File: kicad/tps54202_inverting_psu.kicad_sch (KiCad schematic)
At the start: 16 parts, among them J6 PowerConnector, J7 PowerConnector, J8 PowerConnector, U6 LM2611AMF/NOPB

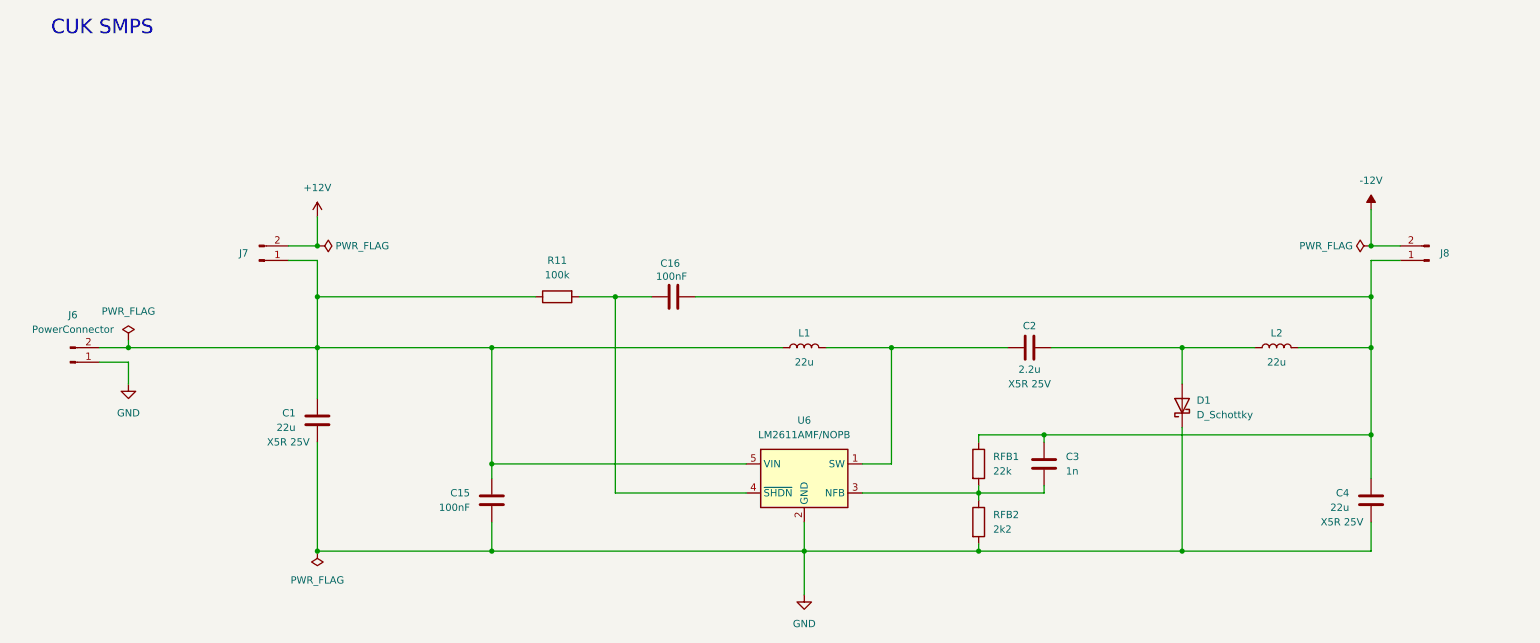
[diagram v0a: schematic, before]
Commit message: updated schematic to use TPS54202
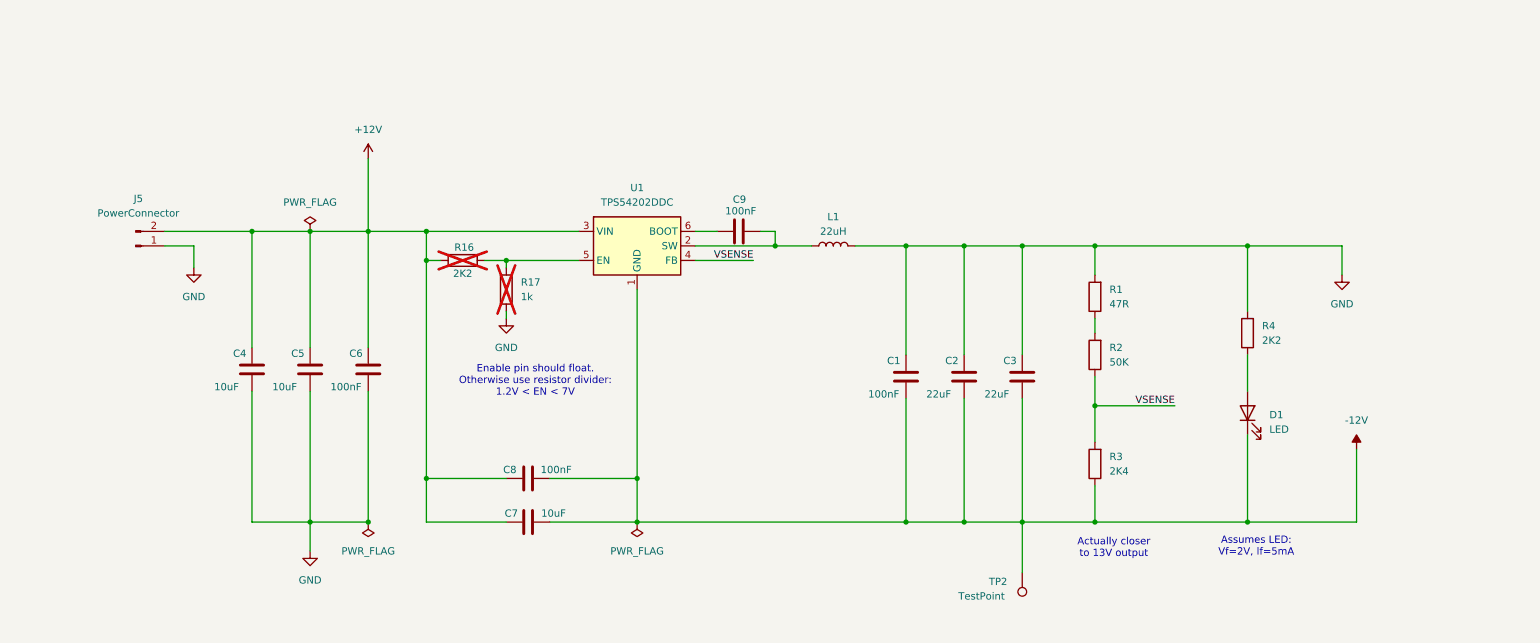
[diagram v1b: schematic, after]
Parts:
- removed C15, C16: 100nF, Capacitor_SMD:C_0603_1608Metric_Pad1.08x0.95mm_HandSolder, symbol Device:C
- removed D1: D_Schottky, Diode_SMD:D_PowerDI-123, symbol Device:D_Schottky
- removed J6: PowerConnector, Connector_Molex:Molex_KK-254_AE-6410-02A_1x02_P2.54mm_Vertical, symbol Connector:Conn_01x02_Pin
- removed J7, J8: PowerConnector, Connector_PinHeader_2.54mm:PinHeader_1x02_P2.54mm_Vertical, symbol Connector:Conn_01x02_Pin
- removed L2: 22u, Inductor_SMD:L_Ferrocore_DLG-0403, symbol Device:L
- removed R11: 100k, Resistor_SMD:R_0805_2012Metric_Pad1.20x1.40mm_HandSolder, symbol Device:R
- removed RFB1: 22k, Resistor_SMD:R_0805_2012Metric_Pad1.20x1.40mm_HandSolder, symbol Device:R
- removed RFB2: 2k2, Resistor_SMD:R_0805_2012Metric_Pad1.20x1.40mm_HandSolder, symbol Device:R
- removed U6: LM2611AMF/NOPB, Package_TO_SOT_SMD:SOT-23-5, symbol Regulator_Switching:LM2611xMF
- added C5, C7: 10uF, Capacitor_SMD:C_0805_2012Metric_Pad1.18x1.45mm_HandSolder, symbol Device:C
- added C6, C8, C9: 100nF, Capacitor_SMD:C_0805_2012Metric_Pad1.18x1.45mm_HandSolder, symbol Device:C
- added D1: LED, LED_SMD:LED_1206_3216Metric_Pad1.42x1.75mm_HandSolder, symbol Device:LED
- added J5: PowerConnector, Connector_Molex:Molex_KK-254_AE-6410-02A_1x02_P2.54mm_Vertical, symbol Connector:Conn_01x02_Pin
- added R1: 47R, Resistor_SMD:R_0805_2012Metric_Pad1.20x1.40mm_HandSolder, symbol Device:R
- added R16, R4: 2K2, Resistor_SMD:R_0805_2012Metric_Pad1.20x1.40mm_HandSolder, symbol Device:R
- added R17: 1k, Resistor_SMD:R_0805_2012Metric_Pad1.20x1.40mm_HandSolder, symbol Device:R
- added R2: 50K, Resistor_SMD:R_0805_2012Metric_Pad1.20x1.40mm_HandSolder, symbol Device:R
- added R3: 2K4, Resistor_SMD:R_0805_2012Metric_Pad1.20x1.40mm_HandSolder, symbol Device:R
- added TP2: TestPoint, TestPoint:TestPoint_Pad_2.5x2.5mm, symbol Connector:TestPoint
- added U1: TPS54202DDC, Package_TO_SOT_SMD:SOT-23-6, symbol Regulator_Switching:TPS54202DDC
- C1: value 22u -> 100nF; footprint Capacitor_SMD:C_1210_3225Metric_Pad1.33x2.70mm_HandSolder -> Capacitor_SMD:C_0805_2012Metric_Pad1.18x1.45mm_HandSolder; LCSC C52306 -> (none); Mouser 187-CL32A226KAJNNNE -> (none); Notes X5R 25V -> (none)
- C2: value 2.2u -> 22uF; footprint Capacitor_SMD:C_1210_3225Metric_Pad1.33x2.70mm_HandSolder -> Capacitor_SMD:C_0805_2012Metric_Pad1.18x1.45mm_HandSolder; LCSC C3841146 -> (none); Mouser 581-12103D225K -> (none); Notes X5R 25V -> (none)
- C3: value 1n -> 22uF; LCSC C15177 -> (none); Mouser 187-CL21B102JCANNNC -> (none); Notes X7R 100V -> (none)
- C4: value 22u -> 10uF; footprint Capacitor_SMD:C_1210_3225Metric_Pad1.33x2.70mm_HandSolder -> Capacitor_SMD:C_0805_2012Metric_Pad1.18x1.45mm_HandSolder; LCSC C52306 -> (none); Mouser 187-CL32A226KAJNNNE -> (none); Notes X5R 25V -> (none)
- L1: value 22u -> 22uH; footprint Inductor_SMD:L_Ferrocore_DLG-0403 -> Inductor_SMD:L_Bourns-SRN8040_8x8.15mm; LCSC C2929420 -> (none); Mouser 815-ASPI-4020S-220MT -> (none); Notes 270mΩ 600mA -> (none)
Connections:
- net +12V: now also C4.1, C5.1, C6.1, C7.1, C8.1, J5.2 (Pin_2), R16.2, U1.3 (VIN)
- net -12V: now also C1.2, C2.2, C3.2, C7.2, C8.2, D1.1 (K), R3.1, TP2.1, U1.1 (GND)
- net GND: now also C2.1, C3.1, C4.2, L1.2, C5.2, C6.2, J5.1 (Pin_1), R1.2, R17.1, R4.2; no longer C4.1
- net at L1.1: now also C9.2, U1.2 (SW); no longer C1.2
- new net: R1.1, R2.2
- new net: D1.2 (A), R4.1
- new net: R16.1, R17.2, U1.5 (EN)
- new net: C9.1, U1.6 (BOOT)
- new net VSENSE: R2.1, R3.2, U1.4 (FB)
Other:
- note added: "Actually closer to 13V output"
- note added: "Assumes LED: Vf=2V, If=5mA"
- note added: "Enable pin should float. Otherwise use resistor divider: 1.2V < EN < 7V"
- note removed: "CUK SMPS"

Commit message: Added extra output capacitor footprints to psu
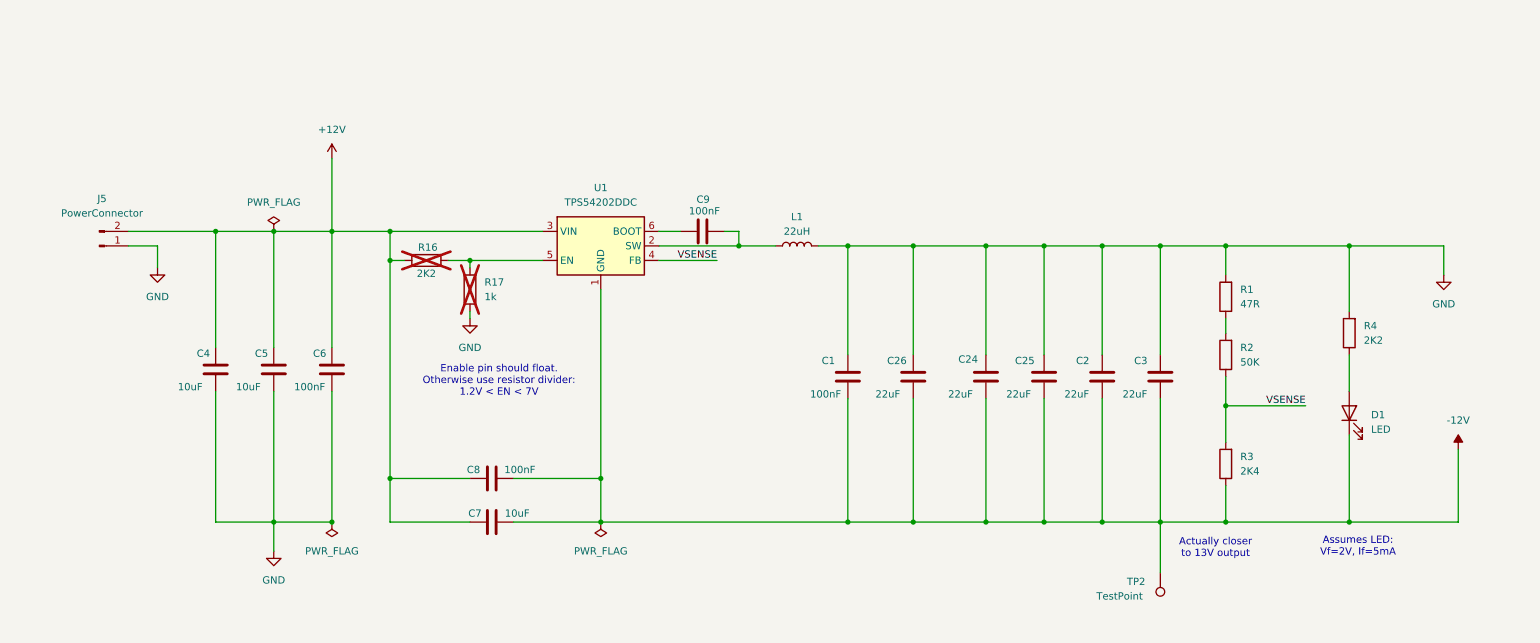
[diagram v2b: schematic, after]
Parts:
- added C24, C25, C26: 22uF, Capacitor_SMD:C_0805_2012Metric_Pad1.18x1.45mm_HandSolder, symbol Device:C
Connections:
- net -12V: now also C24.2, C25.2, C26.2
- net GND: now also C24.1, C25.1, C26.1
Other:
- moved on the sheet: C1, C2, C3, C4, C5, C6, C7, C8, C9, D1, J5, L1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

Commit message: Finished RevC layout
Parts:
- removed R1: 47R, Resistor_SMD:R_0805_2012Metric_Pad1.20x1.40mm_HandSolder, symbol Device:R
- removed R16: 2K2, Resistor_SMD:R_0805_2012Metric_Pad1.20x1.40mm_HandSolder, symbol Device:R
- removed R17: 1k, Resistor_SMD:R_0805_2012Metric_Pad1.20x1.40mm_HandSolder, symbol Device:R
- removed TP2: TestPoint, TestPoint:TestPoint_Pad_2.5x2.5mm, symbol Connector:TestPoint
- L1: footprint Inductor_SMD:L_Bourns-SRN8040_8x8.15mm -> Inductor_SMD:L_Ferrocore_DLG-0403
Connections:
- net GND: now also R2.2
- no-connect marks 0 -> 1
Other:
- company: (none) -> Created By: ${AUTHOR}
- title: (none) -> ${PROJECTNAME}
- moved on the sheet: R2, R3

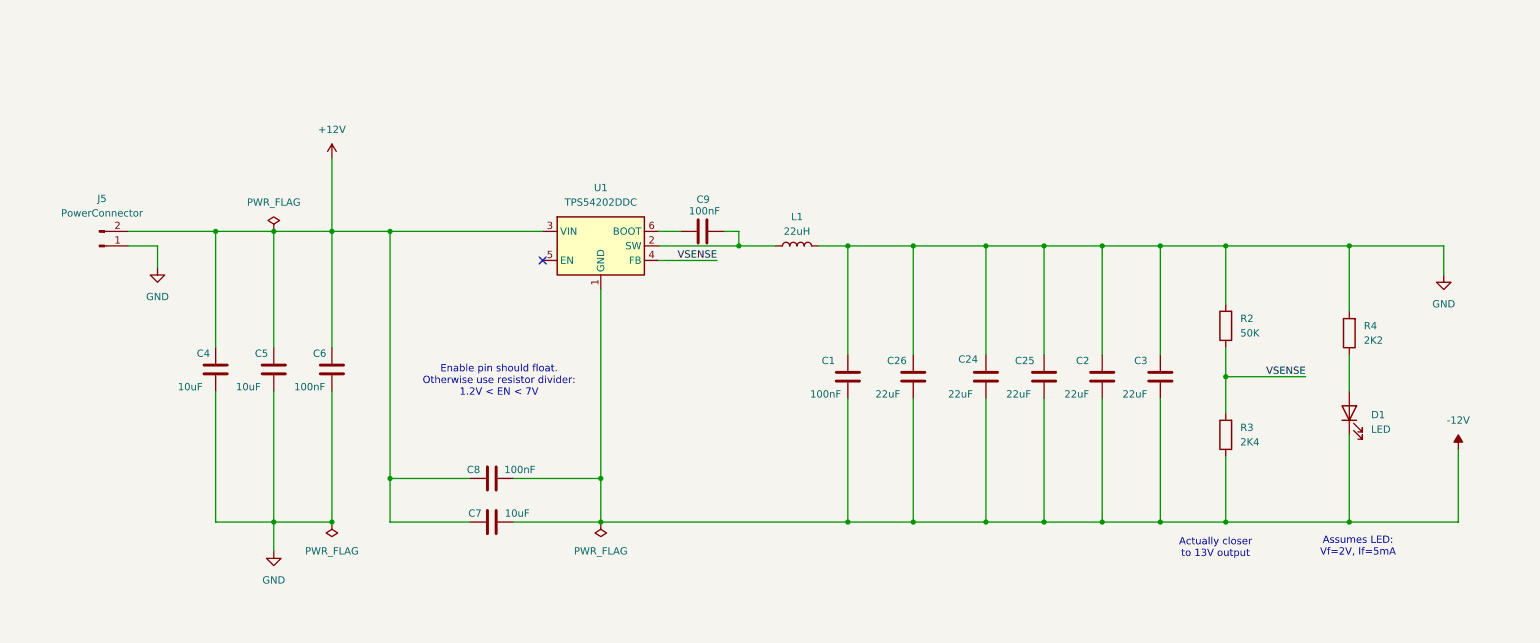
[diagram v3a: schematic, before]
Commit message: changed voltage rails to +/-5V; changed PSU feedback resistor to provide -5V
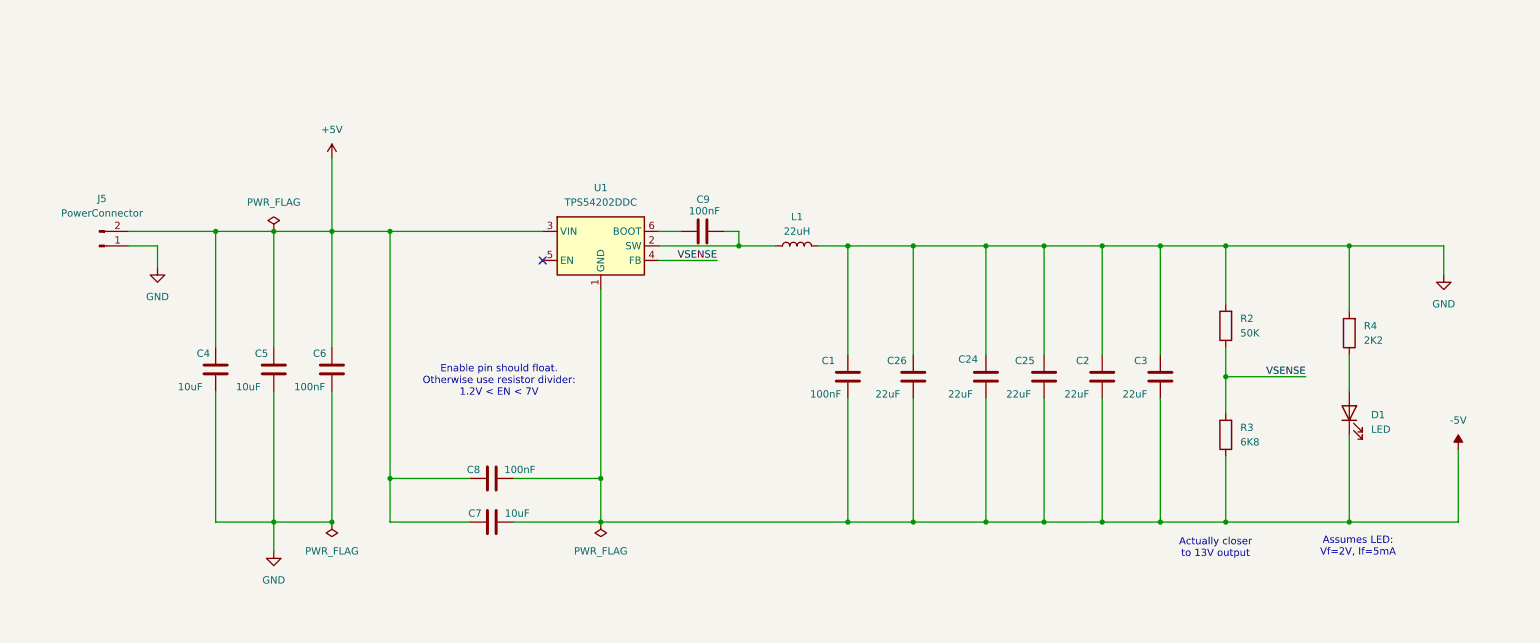
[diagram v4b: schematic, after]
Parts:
- R3: value 2K4 -> 6K8
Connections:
- net +12V renamed +5V
- net -12V renamed -5V
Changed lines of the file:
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@@
 			)
 		)
-		(property "Value" "2K4"
+		(property "Value" "6K8"
 			(at 229.87 95.2499 0)
 			(effects
@@
 	)
 	(symbol
-		(lib_id "power:+12V")
-		(at 71.12 45.72 0)
-		(unit 1)
-		(exclude_from_sim no)
-		(in_bom yes)
-		(on_board yes)
-		(dnp no)
-		(fields_autoplaced yes)
-		(property "Reference" "#PWR027"
-			(at 71.12 49.53 0)
-			(effects
-				(font
-					(size 1.27 1.27)
-				)
-				(hide yes)
-			)
-		)
-		(property "Value" "+12V"
-			(at 71.12 40.64 0)
-			(effects
-				(font
-					(size 1.27 1.27)
-				)
-			)
-		)
-		(property "Footprint" ""
-			(at 71.12 45.72 0)
-			(effects
-				(font
-					(size 1.27 1.27)
-				)
-				(hide yes)
-			)
-		)
-		(property "Datasheet" ""
-			(at 71.12 45.72 0)
-			(effects
-				(font
-					(size 1.27 1.27)
-				)
-				(hide yes)
-			)
-		)
-		(property "Description" "Power symbol creates a global label with name \"+12V\""
-			(at 71.12 45.72 0)
-			(effects
-				(font
-					(size 1.27 1.27)
-				)
-				(hide yes)
-			)
-		)
-		(pin "1"
-		)
-		(instances
-			(project "Tiny4xPoweredStereoMixer"
-				(path "/68c4b081-ef47-4ba5-a55f-4ef66cb2b598/94012ff5-5e55-42ff-bfc1-d0e6ccd3728b"
-					(reference "#PWR027")
-					(unit 1)
-				)
-			)
-		)
-	)
-	(symbol
 		(lib_id "power:GND")
 		(at 60.96 114.3 0)
@@
 	)
 	(symbol
+		(lib_id "power:-5V")
+		(at 267.97 96.52 0)
+		(unit 1)
+		(exclude_from_sim no)
+		(in_bom yes)
+		(on_board yes)
+		(dnp no)
+		(fields_autoplaced yes)
+		(property "Reference" "#PWR05"
+			(at 267.97 100.33 0)
+			(effects
+				(font
+					(size 1.27 1.27)
+				)
+				(hide yes)
+			)
+		)
+		(property "Value" "-5V"
+			(at 267.97 91.44 0)
+			(effects
+				(font
+					(size 1.27 1.27)
+				)
+			)
+		)
+		(property "Footprint" ""
+			(at 267.97 96.52 0)
+			(effects
+				(font
+					(size 1.27 1.27)
+				)
+				(hide yes)
+			)
+		)
+		(property "Datasheet" ""
+			(at 267.97 96.52 0)
+			(effects
+				(font
+					(size 1.27 1.27)
+				)
+				(hide yes)
+			)
+		)
+		(property "Description" "Power symbol creates a global label with name \"-5V\""
+			(at 267.97 96.52 0)
+			(effects
+				(font
+					(size 1.27 1.27)
+				)
+				(hide yes)
+			)
+		)
+		(pin "1"
+		)
+		(instances
+			(project "Tiny4xPoweredStereoMixer"
+				(path "/68c4b081-ef47-4ba5-a55f-4ef66cb2b598/94012ff5-5e55-42ff-bfc1-d0e6ccd3728b"
+					(reference "#PWR05")
+					(unit 1)
+				)
+			)
+		)
+	)
+	(symbol
 		(lib_id "Device:L")
 		(at 152.4 60.96 90)
@@
 	)
 	(symbol
+		(lib_id "power:+5V")
+		(at 71.12 45.72 0)
+		(unit 1)
+		(exclude_from_sim no)
+		(in_bom yes)
+		(on_board yes)
+		(dnp no)
+		(fields_autoplaced yes)
+		(property "Reference" "#PWR06"
+			(at 71.12 49.53 0)
+			(effects
+				(font
+					(size 1.27 1.27)
+				)
+				(hide yes)
+			)
+		)
+		(property "Value" "+5V"
+			(at 71.12 40.64 0)
+			(effects
+				(font
+					(size 1.27 1.27)
+				)
+			)
+		)
+		(property "Footprint" ""
+			(at 71.12 45.72 0)
+			(effects
+				(font
+					(size 1.27 1.27)
+				)
+				(hide yes)
+			)
+		)
+		(property "Datasheet" ""
+			(at 71.12 45.72 0)
+			(effects
+				(font
+					(size 1.27 1.27)
+				)
+				(hide yes)
+			)
+		)
+		(property "Description" "Power symbol creates a global label with name \"+5V\""
+			(at 71.12 45.72 0)
+			(effects
+				(font
+					(size 1.27 1.27)
+				)
+				(hide yes)
+			)
+		)
+		(pin "1"
+		)
+		(instances
+			(project "Tiny4xPoweredStereoMixer"
+				(path "/68c4b081-ef47-4ba5-a55f-4ef66cb2b598/94012ff5-5e55-42ff-bfc1-d0e6ccd3728b"
+					(reference "#PWR06")
+					(unit 1)
+				)
+			)
+		)
+	)
+	(symbol
 		(lib_id "power:GND")
 		(at 265.43 66.04 0)
@@
 					(unit 1)
 				)
-			)
-		)
-	)
-	(symbol
-		(lib_id "power:-12V")
-		(at 267.97 96.52 0)
-		(unit 1)
-		(exclude_from_sim no)
-		(in_bom yes)
-		(on_board yes)
-		(dnp no)
-		(fields_autoplaced yes)
-		(property "Reference" "#PWR031"
-			(at 267.97 100.33 0)
-			(effects
-				(font
-					(size 1.27 1.27)
-				)
-				(hide yes)
-			)
-		)
-		(property "Value" "-12V"
-			(at 267.97 91.44 0)
-			(effects
-				(font
-					(size 1.27 1.27)
-				)
-			)
-		)
-		(property "Footprint" ""
-			(at 267.97 96.52 0)
-			(effects
-				(font
-					(size 1.27 1.27)
-				)
-				(hide yes)
-			)
-		)
-		(property "Datasheet" ""
-			(at 267.97 96.52 0)
-			(effects
-				(font
-					(size 1.27 1.27)
-				)
-				(hide yes)
-			)
-		)
-		(property "Description" "Power symbol creates a global label with name \"-12V\""
-			(at 267.97 96.52 0)
-			(effects
-				(font
-					(size 1.27 1.27)
-				)
-				(hide yes)
-			)
-		)
-		(pin "1"
-		)
-		(instances
-			(project "Tiny4xPoweredStereoMixer"
-				(path "/68c4b081-ef47-4ba5-a55f-4ef66cb2b598/94012ff5-5e55-42ff-bfc1-d0e6ccd3728b"
-					(reference "#PWR031")
-					(unit 1)
-				)
